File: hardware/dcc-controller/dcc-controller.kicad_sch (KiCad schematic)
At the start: 45 parts

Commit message: Inital layout
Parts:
- added H1, H2, H3, H4: MountingHole, MountingHole:MountingHole_3.2mm_M3, symbol Mechanical:MountingHole
- C1, C2, C3, C4, C6, C8, C9: renamed from C?; footprint (none) -> Capacitor_SMD:C_0805_2012Metric
- C10, C5, C7: renamed from C?; footprint (none) -> Capacitor_THT:CP_Radial_D5.0mm_P2.50mm
- D1: renamed from D?; value LED -> 1F; footprint (none) -> LED_SMD:LED_0805_2012Metric
- D2: renamed from D?; value LED -> 1R; footprint (none) -> LED_SMD:LED_0805_2012Metric
- D3: renamed from D?; value LED -> 2F; footprint (none) -> LED_SMD:LED_0805_2012Metric
- D4: renamed from D?; value LED -> 2R; footprint (none) -> LED_SMD:LED_0805_2012Metric
- D5: renamed from D?; value LED -> PROG; footprint (none) -> LED_SMD:LED_0805_2012Metric
- D6: renamed from D?; value LED -> ALARM; footprint (none) -> LED_SMD:LED_0805_2012Metric
- D7: renamed from D?; value LED -> PWR; footprint (none) -> LED_SMD:LED_0805_2012Metric
- D8: renamed from D?; footprint (none) -> LED_SMD:LED_0805_2012Metric
- F1: renamed from F?; footprint (none) -> Fuse:Fuse_Blade_ATO_directSolder
- IC1: renamed from IC?; footprint SON50P200X200X80-9N -> Package_SON:WSON-8-1EP_2x2mm_P0.5mm_EP0.9x1.6mm
- J1: renamed from J?; footprint (none) -> TerminalBlock:TerminalBlock_bornier-4_P5.08mm
- R1, R2, R3, R4, R5, R6, R7, R8, R9: renamed from R?; footprint (none) -> Resistor_SMD:R_0805_2012Metric
- RV1, RV2: renamed from RV?; footprint (none) -> potentiometer:potentiometer vertical
- SW1, SW5: renamed from SW?; footprint (none) -> Package_DIP:DIP-14_W7.62mm_Socket
- SW2, SW3: renamed from SW?; footprint (none) -> Button_Switch_THT:SW_PUSH_6mm_H5mm
- SW4: renamed from SW?; footprint (none) -> dp3t:dp3t
- SW6: renamed from SW?; value SW_SPST -> SW_PWR; footprint (none) -> Connector_PinHeader_2.54mm:PinHeader_1x03_P2.54mm_Vertical
- U1: renamed from U?; footprint Package_QFP:LQFP-48_7x7mm_P0.5mm -> stm32f103c6t6-blue-pill:stm32-blue-pill
- U2: renamed from U?; footprint (none) -> Package_SO:SOIC-14_3.9x8.7mm_P1.27mm
- U3: renamed from U?; footprint (none) -> Package_TO_SOT_THT:TO-220-3_Vertical
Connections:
- net E_STOP: now also U1.23 (PB14); no longer U1.9 (PA4)
- net GND: now also U2.12, U2.8, U2.9
- net LED_1F: now also U1.10 (PA5); no longer U1.5 (PA0)
- net LED_1R: now also U1.11 (PA6); no longer U1.6 (PA1)
- net LED_2F: now also U1.5 (PA0); no longer U1.7 (PA2)
- net LED_2R: now also U1.6 (PA1); no longer U1.8 (PA3)
- net LED_ALARM: now also U1.22 (PB13); no longer U1.21 (PB12)
- net LED_PROG: now also U1.21 (PB12); no longer U1.22 (PB13)
- net OUT_DIR: now also U1.8 (PA3); no longer U1.11 (PA6)
- net OUT_EN: now also U1.7 (PA2); no longer U1.10 (PA5)
- net POT_A: now also U1.14 (PB1); no longer U1.13 (PB0)
- net POT_B: now also U1.13 (PB0); no longer U1.14 (PB1)
- net PROG_BTN: now also U1.9 (PA4); no longer U1.23 (PB14)
- net PROG_MODE_1: now also U1.16 (PB11); no longer U1.15 (PB10)
- net PROG_MODE_2: now also U1.15 (PB10); no longer U1.16 (PB11)
- net IN_1: now reaches U2.3, U2.5
- net IN_1: now also IC1.3 (IN1); no longer IC1.2 (IN2)
- net IN_2: now reaches U2.4
- net IN_2: now also IC1.2 (IN2); no longer IC1.3 (IN1)
- no-connect marks 7 -> 8
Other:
- moved on the sheet: U2C, U2D

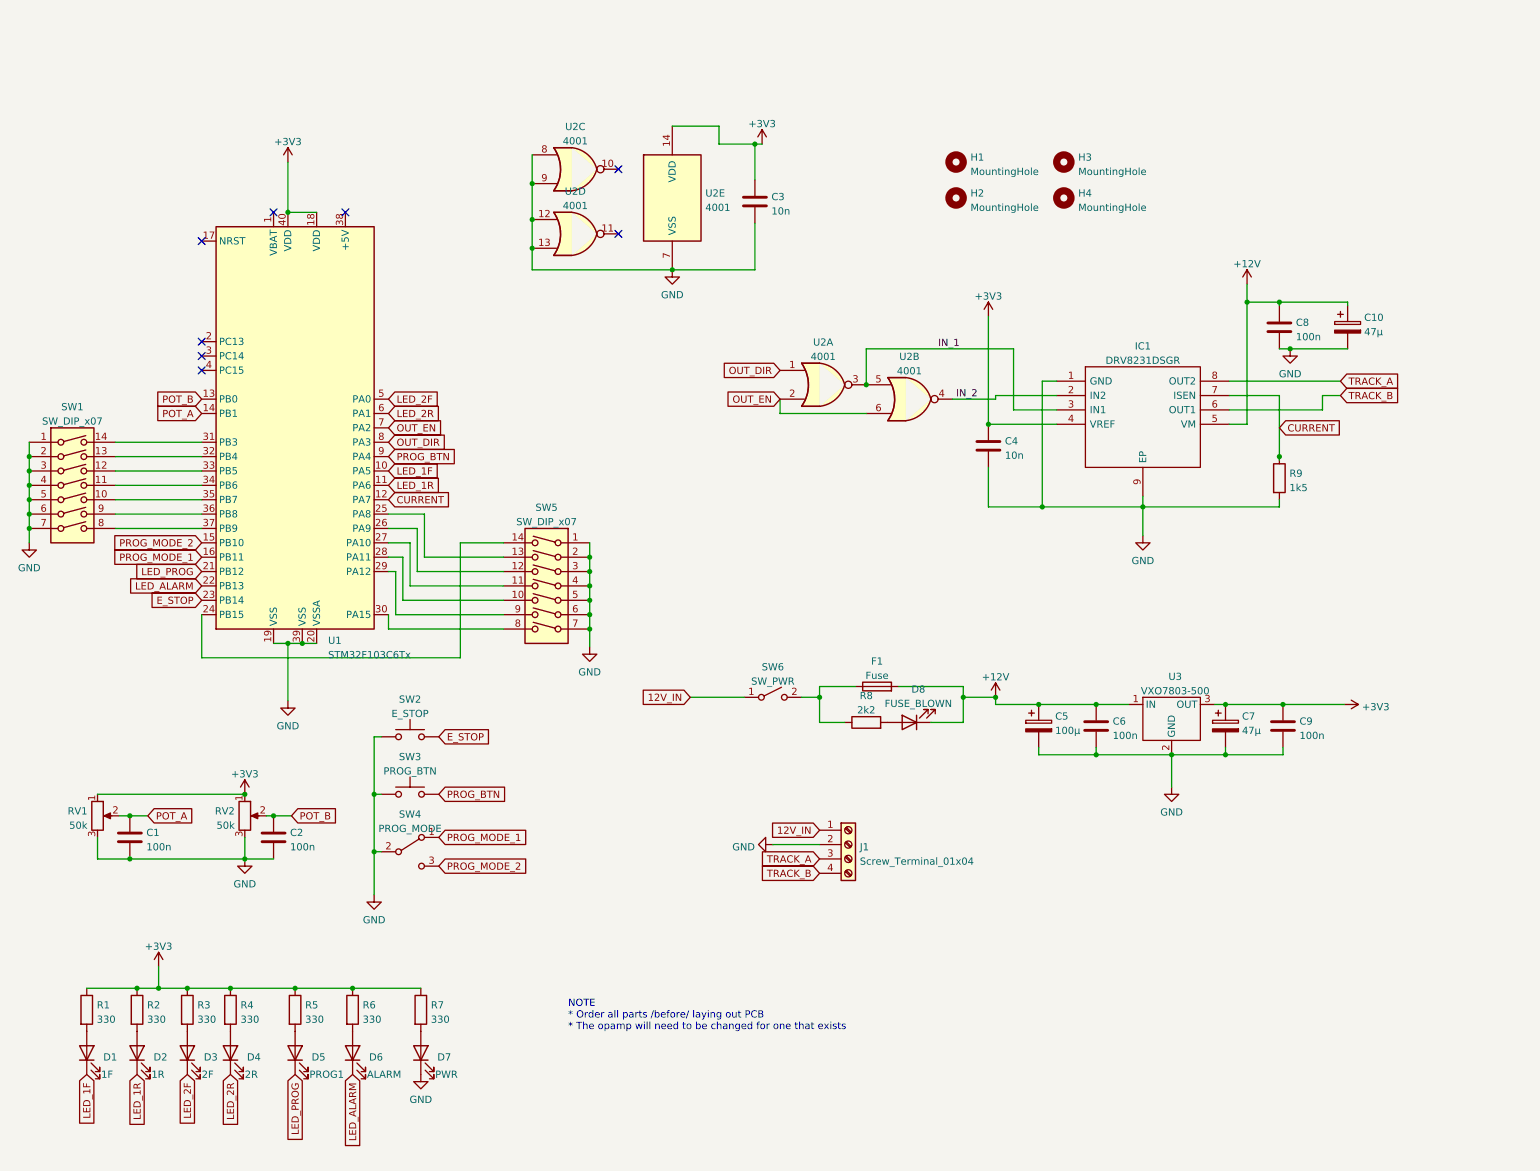
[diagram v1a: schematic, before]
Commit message: Update schematic for display
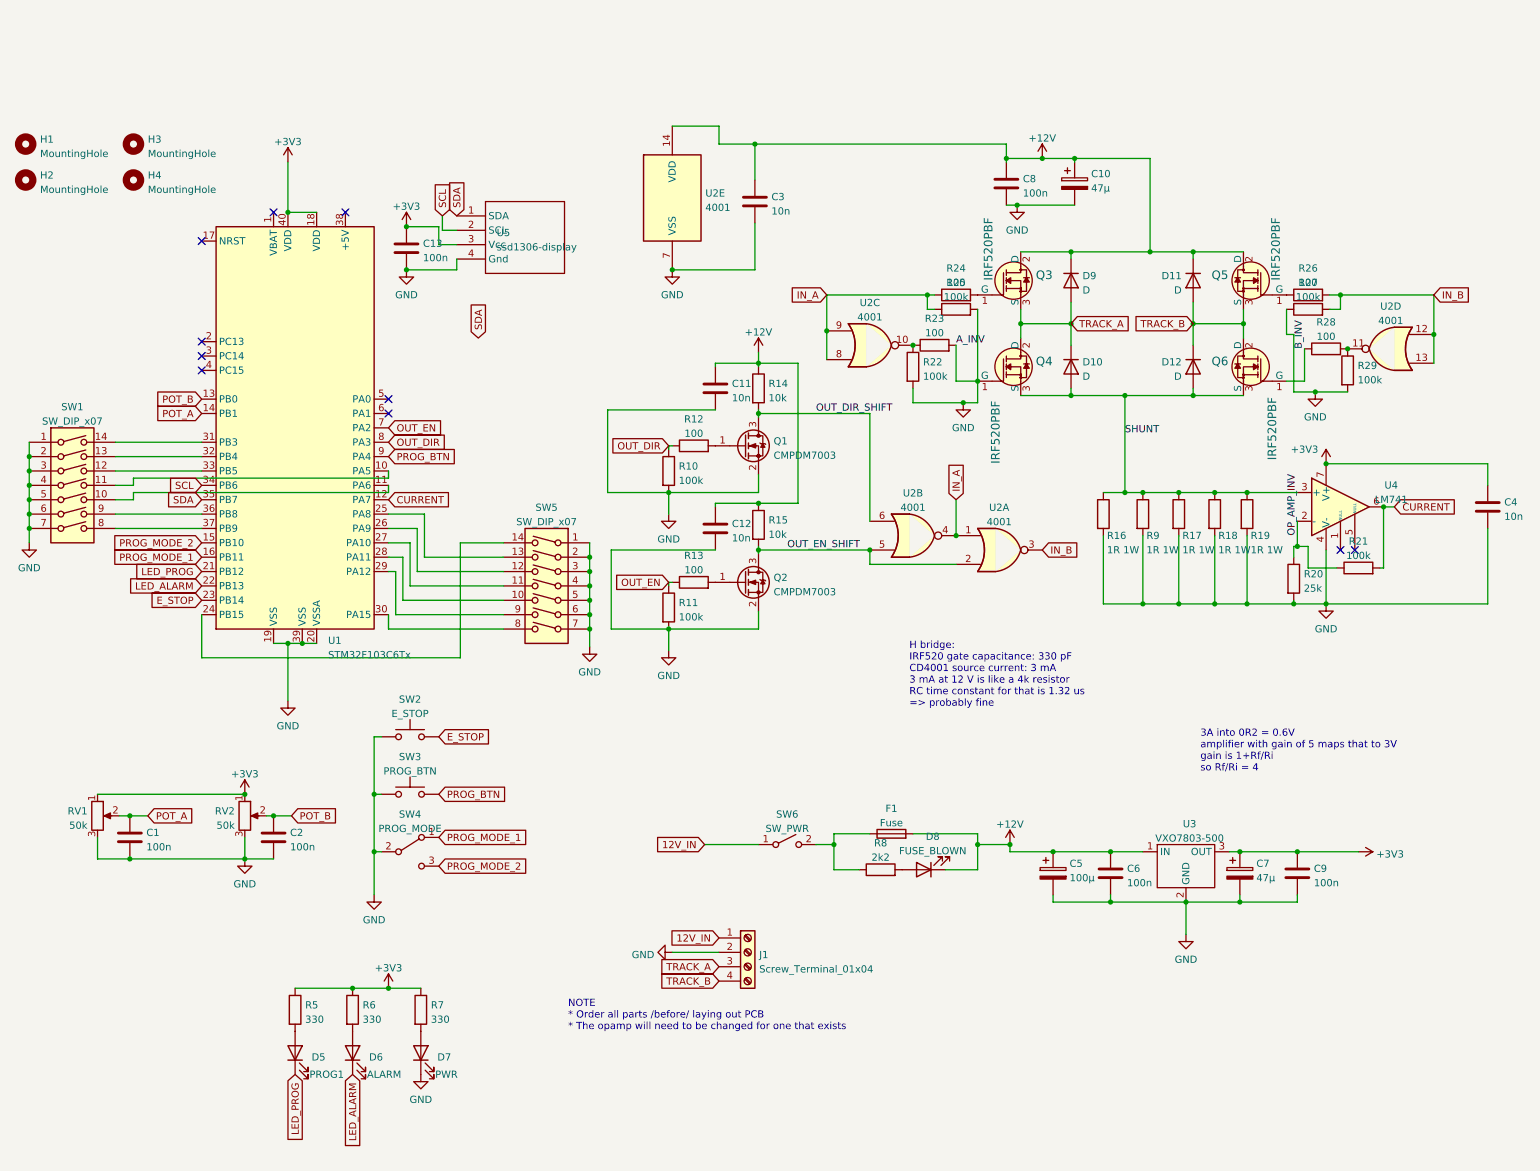
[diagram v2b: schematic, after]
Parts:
- removed D1: 1F, LED_SMD:LED_0805_2012Metric, symbol Device:LED
- removed D2: 1R, LED_SMD:LED_0805_2012Metric, symbol Device:LED
- removed D3: 2F, LED_SMD:LED_0805_2012Metric, symbol Device:LED
- removed D4: 2R, LED_SMD:LED_0805_2012Metric, symbol Device:LED
- removed IC1: DRV8231DSGR, Package_SON:WSON-8-1EP_2x2mm_P0.5mm_EP0.9x1.6mm, symbol DRV8231DSGR:DRV8231DSGR
- removed R1, R2, R3, R4: 330, Resistor_SMD:R_0805_2012Metric, symbol Device:R
- added C11, C12: 10n, Capacitor_SMD:C_0805_2012Metric, symbol Device:C
- added C13: 100n, Capacitor_SMD:C_0805_2012Metric, symbol Device:C
- added D10, D11, D12, D9: D, Diode_SMD:D_MELF, symbol Device:D
- added Q1, Q2: CMPDM7003, Package_TO_SOT_SMD:SOT-23, symbol Transistor_FET:2N7002
- added Q3, Q4, Q5, Q6: IRF520PBF, Package_TO_SOT_THT:TO-220F-3_Vertical, symbol dk_Transistors-FETs-MOSFETs-Single:IRF510PBF
- added R10, R11, R21, R22, R25, R27, R29: 100k, Resistor_SMD:R_0805_2012Metric, symbol Device:R
- added R12, R13, R23, R24, R26, R28: 100, Resistor_SMD:R_0805_2012Metric, symbol Device:R
- added R14, R15: 10k, Resistor_SMD:R_0805_2012Metric, symbol Device:R
- added R16, R17, R18, R19: 1R 1W, Resistor_THT:R_Axial_DIN0207_L6.3mm_D2.5mm_P10.16mm_Horizontal, symbol Device:R
- added R20: 25k, Resistor_SMD:R_0805_2012Metric, symbol Device:R
- added U4: LM741, Package_DIP:DIP-8_W7.62mm, symbol Amplifier_Operational:LM741
- added U5: ssd1306-display, ssd1306-display:ssd1306-display, symbol ssd1306-display:ssd1306-display
- R9: value 1k5 -> 1R 1W; footprint Resistor_SMD:R_0805_2012Metric -> Resistor_THT:R_Axial_DIN0207_L6.3mm_D2.5mm_P10.16mm_Horizontal
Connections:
- net LED_1F is gone; now on an unnamed net: U1.10 (PA5)
- net LED_1R is gone; now on an unnamed net: U1.11 (PA6)
- net +12V: now also C3.1, U2.14 (VDD), C11.1, C12.1, D11.1 (K), D9.1 (K), Q3.2 (D), Q5.2 (D), R14.1, R15.1
- net +3V3: now also C13.1, U4.7 (V+), U5.3 (Vcc); no longer C3.1, U2.14 (VDD)
- net CURRENT: now also R21.2, U4.6; no longer R9.1
- net GND: now also C11.2, C12.2, C13.2, Q1.2 (S), Q2.2 (S), Q4.1 (G), R10.2, R11.2, R16.2, R17.2, R18.2, R19.2, R20.2, R22.2, R23.2, R25.2, R27.1, R29.2, U4.4 (V-), U5.4 (Gnd); no longer U2.12, U2.13, U2.8, U2.9
- net OUT_DIR: now also R10.1, R12.1; no longer U2.1
- net OUT_EN: now also R11.1, R13.1; no longer U2.2, U2.6
- net TRACK_A: now also D10.1 (K), D9.2 (A), Q3.3 (S), Q4.2 (D)
- net TRACK_B: now also D11.2 (A), D12.1 (K), Q5.3 (S), Q6.2 (D)
- net at SW1.10: no longer U1.35 (PB7)
- net at SW1.11: no longer U1.34 (PB6)
- net at U2.10: now also R22.1, R23.1
- net at U2.11: now also R28.2, R29.1
- net IN_1 renamed IN_B
- net IN_B: now also U2.12, U2.13, R26.2, R27.2; no longer U2.5
- net IN_2 renamed IN_A
- net IN_A: now also U2.1, U2.8, U2.9, R24.1, R25.1
- net LED_2F: no longer names the net of U1.5 (PA0)
- net LED_2R: no longer names the net of U1.6 (PA1)
- new net: Q2.1 (G), R13.2
- new net: Q5.1 (G), R26.1
- new net: Q3.1 (G), R24.2
- new net: Q1.1 (G), R12.2
- new net B_INV: Q6.1 (G), R28.1
- new net OP_AMP_INV: R20.1, R21.1, U4.2 (-)
- new net OUT_DIR_SHIFT: Q1.3 (D), R14.2, U2.6
- new net OUT_EN_SHIFT: Q2.3 (D), R15.2, U2.2, U2.5
- new net SCL: U1.34 (PB6), U5.2 (SCL)
- new net SDA: U1.35 (PB7), U5.1 (SDA)
- new net SHUNT: D10.2 (A), D12.2 (A), Q4.3 (S), Q6.3 (S), R16.1, R17.1, R18.1, R19.1, R9.1, U4.3 (+)
- no-connect marks 8 -> 10
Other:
- note added: "3A into 0R2 = 0.6V amplifier with gain of 5 maps that to 3V gain is 1+Rf/Ri so Rf/Ri = 4"
- note added: "H bridge: IRF520 gate capacitance: 330 pF CD4001 source current: 3 mA 3 mA at 12 V is like a 4k resistor RC time constant for that is 1.32 us => probably fine"
- moved on the sheet: C10, C4, C5, C6, C7, C8, C9, D8, F1, H1, H2, H3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

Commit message: Do layout and routing for new display version
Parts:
- removed SW6: SW_PWR, Connector_PinHeader_2.54mm:PinHeader_1x03_P2.54mm_Vertical, symbol Switch:SW_SPST
- added D1: CHAN_A, LED_SMD:LED_0805_2012Metric, symbol Device:LED
- added D2: CHAN_B, LED_SMD:LED_0805_2012Metric, symbol Device:LED
- added R1, R2: 330, Resistor_SMD:R_0805_2012Metric, symbol Device:R
- added SW6: SW_PWR, spdt-slide-switch:spdt-slide-switch, symbol Switch:SW_SPDT
- added TP10, TP11, TP12, TP13, TP14, TP15, TP3, TP4, TP5, TP6, TP7, TP8, TP9: TestPoint, TestPoint:TestPoint_THTPad_D2.0mm_Drill1.0mm, symbol Connector:TestPoint
- F1: footprint Fuse:Fuse_Blade_ATO_directSolder -> automotive-fuse-mount:automotive-fuse-mount
- RV1, RV2: footprint potentiometer:potentiometer vertical -> Potentiometer_THT:Potentiometer_Bourns_PTV09A-1_Single_Vertical
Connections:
- net +12V: now also TP11.1
- net +3V3: now also R1.1, R2.1, TP14.1
- net 12V_IN: now also SW6.2 (B)
- net CURRENT: now also TP5.1
- net GND: now also TP13.1; no longer Q4.1 (G), R23.2
- net IN_A: now also TP8.1
- net IN_B: now also TP15.1
- net OUT_DIR: now also TP4.1
- net OUT_DIR_SHIFT: now also TP9.1
- net OUT_EN: now also TP3.1
- net OUT_EN_SHIFT: now also TP10.1
- net POT_A: now also TP7.1
- net POT_B: now also TP6.1
- net SHUNT: now also TP12.1
- net at SW1.10: now also U1.10 (PA5); no longer U1.11 (PA6)
- net at SW1.11: now also U1.11 (PA6); no longer U1.10 (PA5)
- net at F1.1, R8.1: now also SW6.1 (A)
- net CHAN_B: now reaches U1.5 (PA0)
- net CHAN_B: now also D2.1 (K)
- net CHAN_A: now reaches U1.6 (PA1)
- net CHAN_A: now also D1.1 (K)
- new net: D2.2 (A), R2.2
- new net: D1.2 (A), R1.2
- new net A_INV: Q4.1 (G), R23.2
- no-connect marks 10 -> 9
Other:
- note added: "3A into 0.2R is 1.8W total 360 mW per resistor"

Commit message: Add gerbers and printouts
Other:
- note added: "1"
- note added: "2022-06-26"
- note added: "DCC Controller"
- note added: "DCC Controller David Young github.com/sciguy16/dcc-controller-rs"
- note removed: "NOTE * Order all parts /before/ laying out PCB * The opamp will need to be changed for one that exists"
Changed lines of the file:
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@@
     (stroke (width 0) (type default) (color 0 0 0 0))
+  )
+  (text "DCC Controller" (at 190.5 190.5 0)
+    (effects (font (size 1.27 1.27)) (justify left bottom))
   )
   (text "H bridge:\nIRF520 gate capacitance: 330 pF\nCD4001 source current: 3 mA\n3 mA at 12 V is like a 4k resistor\nRC time constant for that is 1.32 us\n=> probably fine"
@@
     (effects (font (size 1.27 1.27)) (justify left bottom))
   )
-  (text "NOTE\n* Order all parts /before/ laying out PCB\n* The opamp will need to be changed for one that exists"
-    (at 114.3 175.26 0)
+  (text "DCC Controller\nDavid Young\ngithub.com/sciguy16/dcc-controller-rs"
+    (at 185.42 175.26 0)
+    (effects (font (size 1.27 1.27)) (justify left bottom))
+  )
+  (text "2022-06-26" (at 207.645 194.31 0)
     (effects (font (size 1.27 1.27)) (justify left bottom))
   )
@@
     (effects (font (size 1.27 1.27)) (justify left bottom))
   )
+  (text "1" (at 269.24 193.675 0)
+    (effects (font (size 1.27 1.27)) (justify left bottom))
+  )
